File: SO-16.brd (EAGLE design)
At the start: 100 x 80 mm, 6 parts, among them IC2 DG409DY, IC3 MAX3040CWE

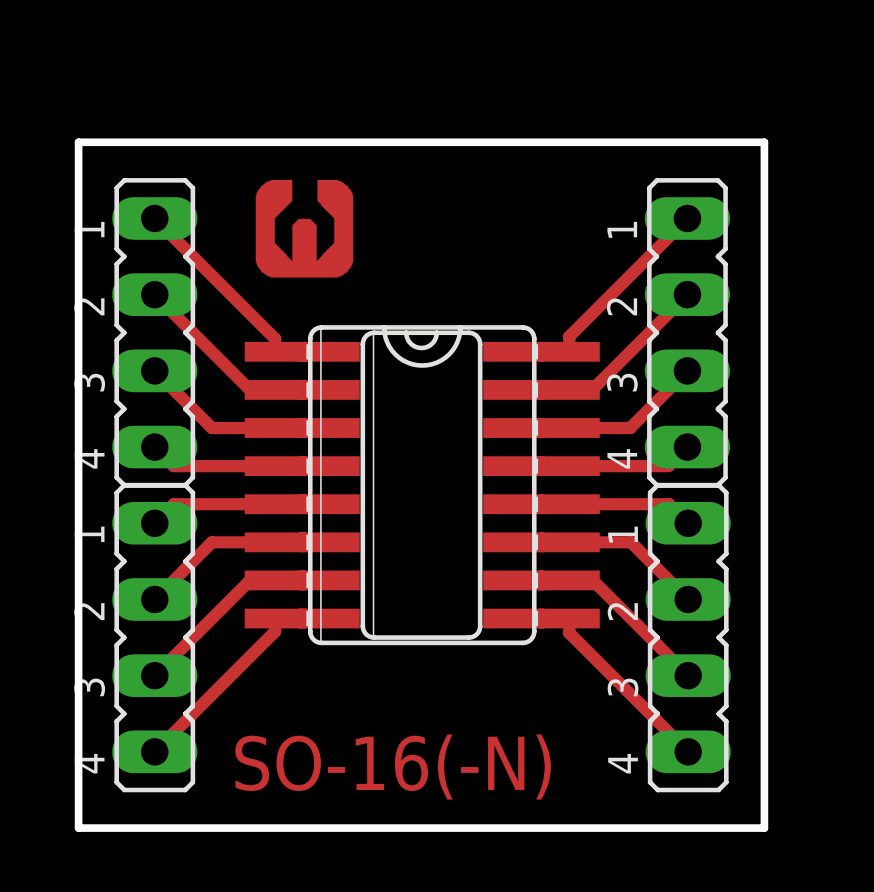
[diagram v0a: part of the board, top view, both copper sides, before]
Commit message: Increase trace clearance
The boards I made had a few shorts.
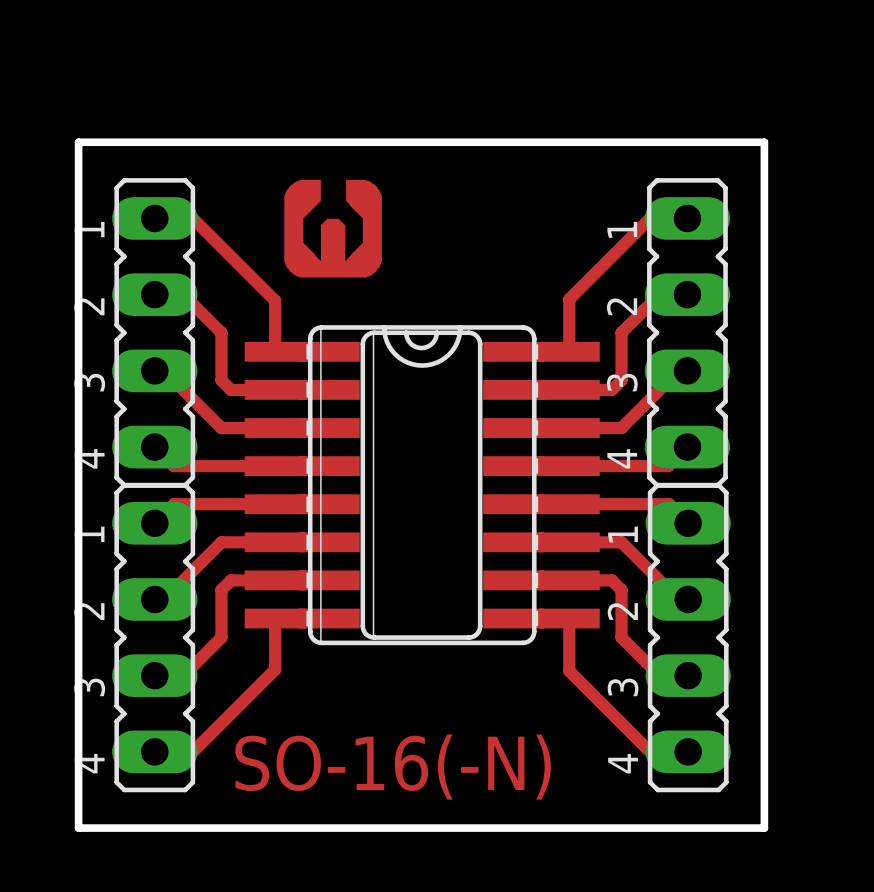
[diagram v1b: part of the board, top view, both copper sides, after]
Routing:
- net N$22: track 7.11 -> 8.04 mm
- net N$19: track 7.13 -> 8.06 mm
- net N$15: track 7.13 -> 8.06 mm
- net N$11: track 7.13 -> 8.06 mm
- net N$18: track 7.94 -> 8.68 mm
- net N$16: track 7.91 -> 8.65 mm
- net N$8: track 7.91 -> 8.65 mm
- net N$25: track 7.93 -> 8.66 mm
